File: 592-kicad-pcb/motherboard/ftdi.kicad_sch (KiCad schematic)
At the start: 43 parts, among them J14 USB_B_Micro, U10 FT4232H, U11 74HC595, Y3 12M

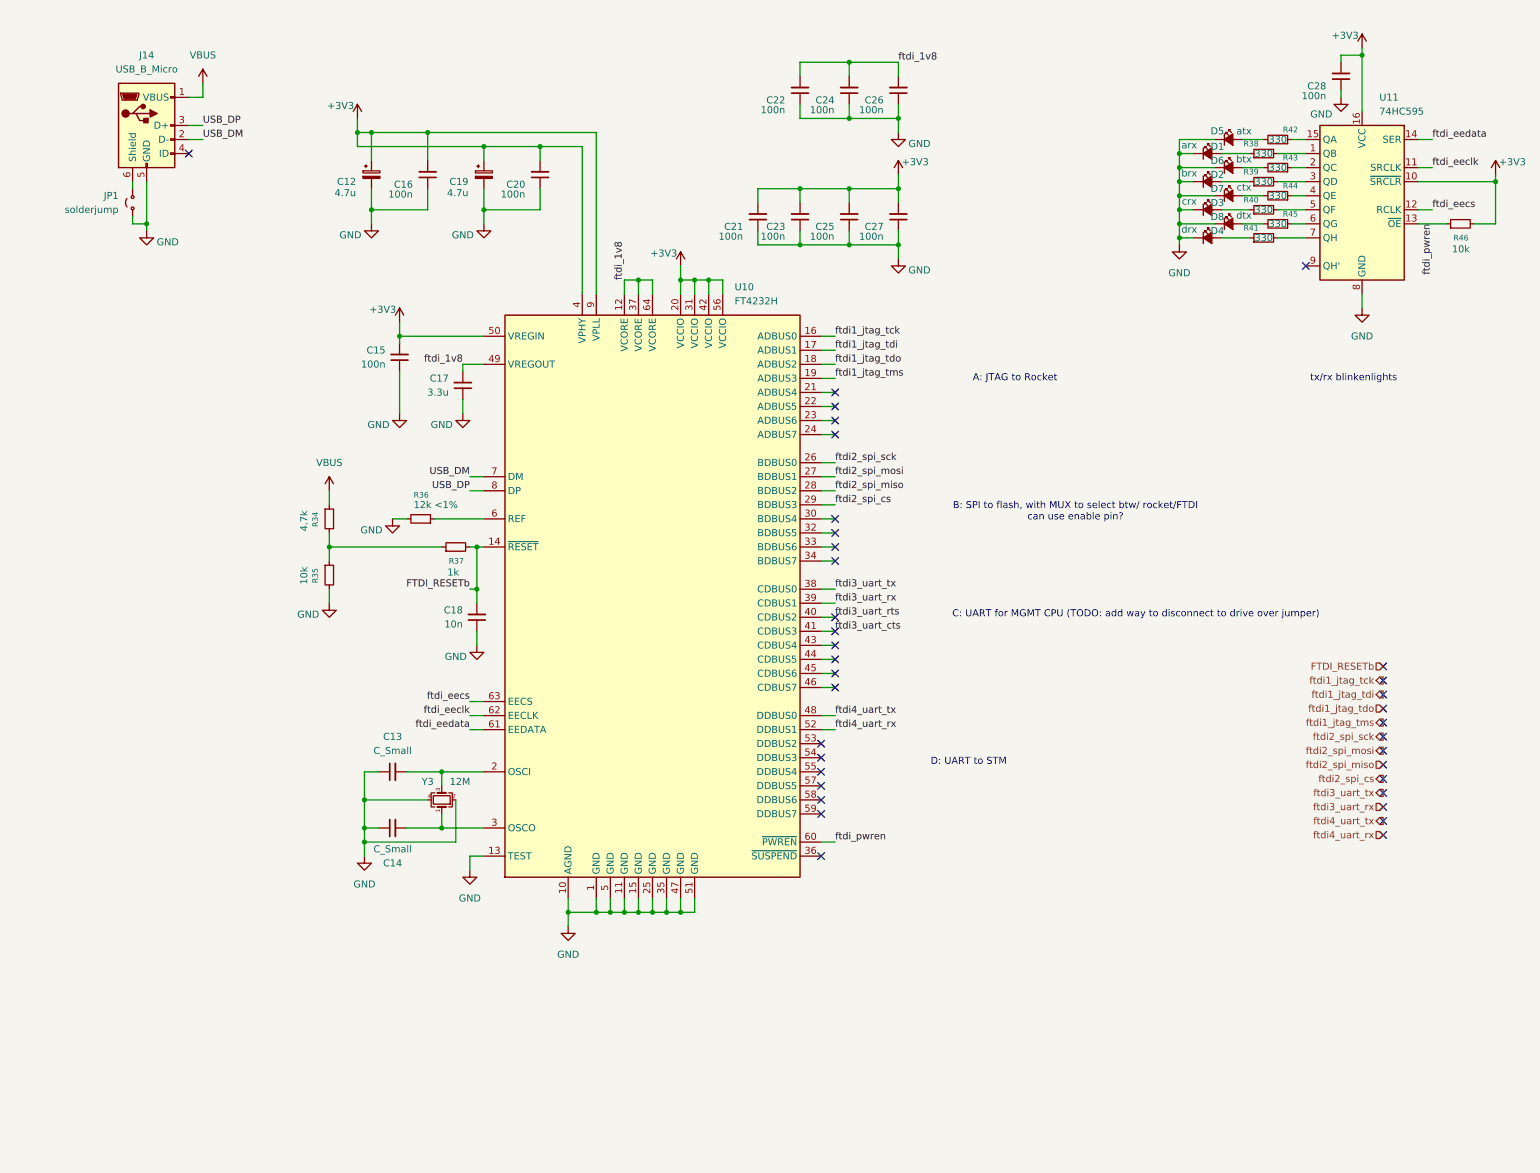
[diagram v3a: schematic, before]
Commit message: add JLC part num for parts, footprints
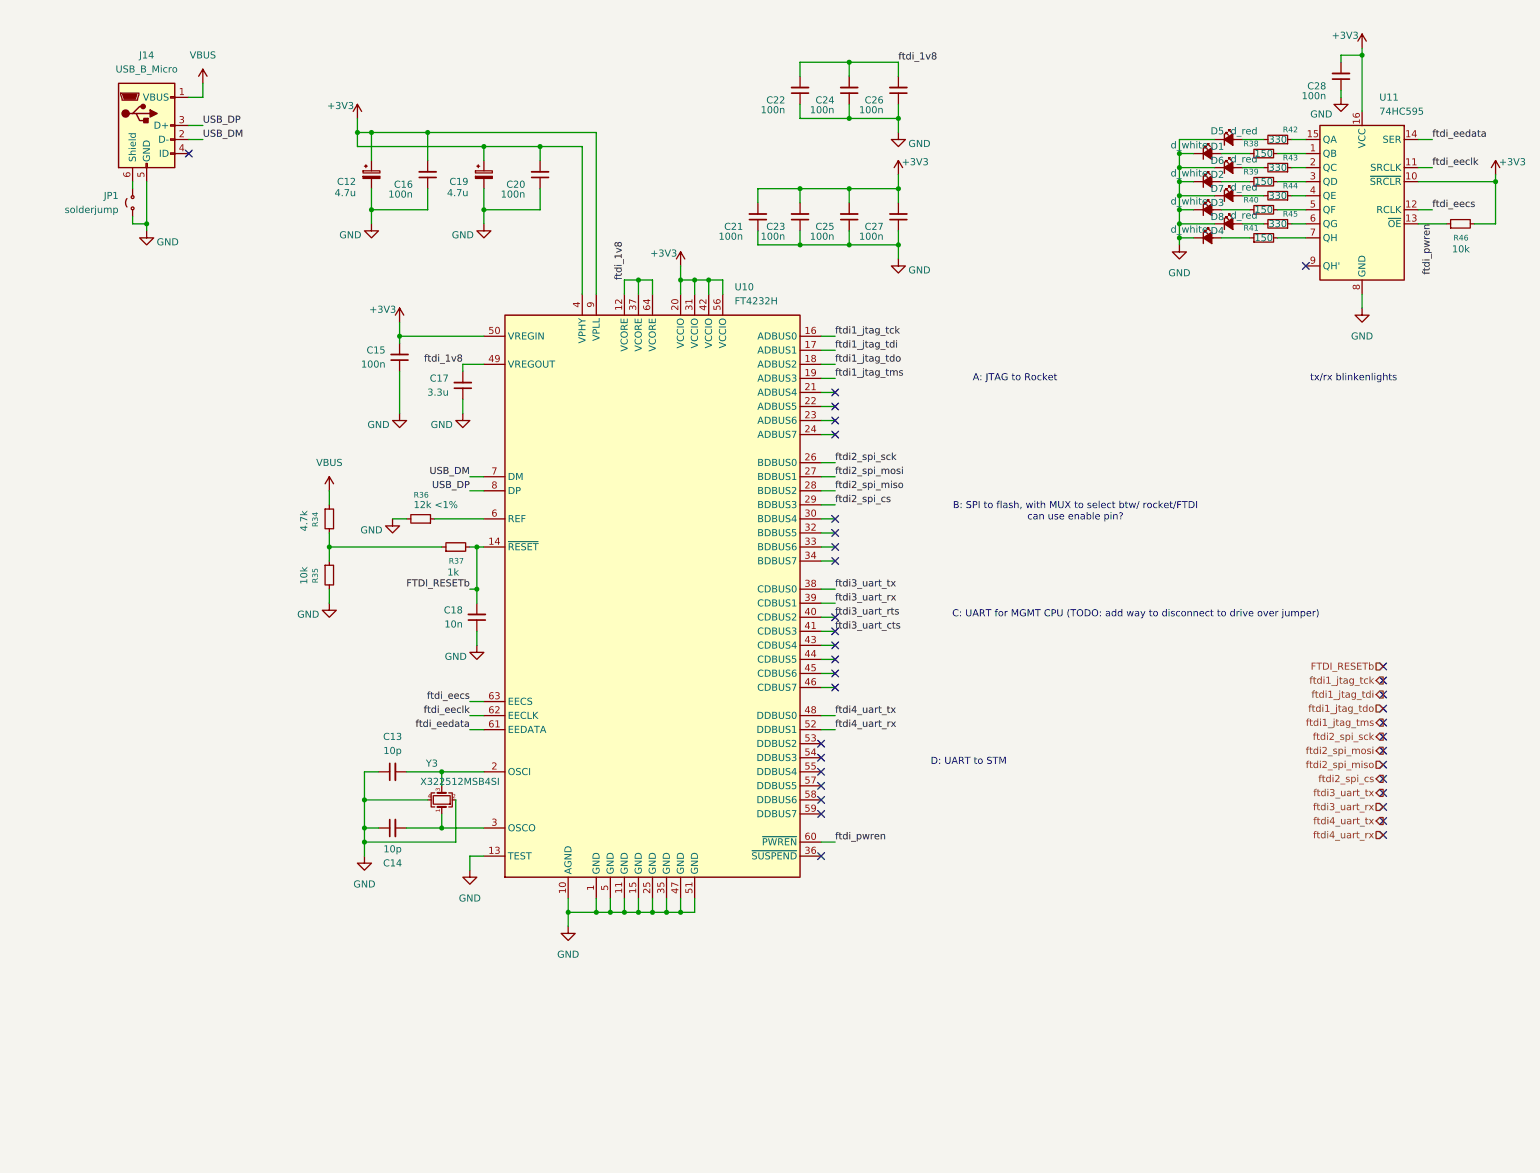
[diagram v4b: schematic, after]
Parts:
- C12, C19: footprint (none) -> Capacitor_Tantalum_SMD:CP_EIA-3216-18_Kemet-A; LCSC (none) -> C7187
- C13, C14: value C_Small -> 10p; footprint (none) -> Capacitor_SMD:C_0402_1005Metric; LCSC (none) -> C32949
- C15, C16, C20, C21, C22, C23, C24, C25, C26, C27, C28: footprint (none) -> Capacitor_SMD:C_0402_1005Metric; LCSC (none) -> C1525
- C17: footprint (none) -> Capacitor_SMD:C_0603_1608Metric; LCSC (none) -> C1588
- C18: footprint (none) -> Capacitor_SMD:C_0402_1005Metric; LCSC (none) -> C15195
- D1: value arx -> d_white; footprint (none) -> Diode_SMD:D_0603_1608Metric; LCSC (none) -> C2290
- D2: value brx -> d_white; footprint (none) -> Diode_SMD:D_0603_1608Metric; LCSC (none) -> C2290
- D3: value crx -> d_white; footprint (none) -> Diode_SMD:D_0603_1608Metric; LCSC (none) -> C2290
- D4: value drx -> d_white; footprint (none) -> Diode_SMD:D_0603_1608Metric; LCSC (none) -> C2290
- D5: value atx -> d_red; footprint (none) -> Diode_SMD:D_0603_1608Metric; LCSC (none) -> C2286
- D6: value btx -> d_red; footprint (none) -> Diode_SMD:D_0603_1608Metric; LCSC (none) -> C2286
- D7: value ctx -> d_red; footprint (none) -> Diode_SMD:D_0603_1608Metric; LCSC (none) -> C2286
- D8: value dtx -> d_red; footprint (none) -> Diode_SMD:D_0603_1608Metric; LCSC (none) -> C2286
- J14: footprint (none) -> Connector_USB:USB_Micro-B_Wuerth_629105150521; LCSC (none) -> C2894326
- JP1: footprint (none) -> Jumper:SolderJumper-2_P1.3mm_Open_RoundedPad1.0x1.5mm
- R34: footprint (none) -> Resistor_SMD:R_0402_1005Metric; LCSC (none) -> C25900
- R35, R46: footprint (none) -> Resistor_SMD:R_0402_1005Metric; LCSC (none) -> C25744
- R36: footprint (none) -> Resistor_SMD:R_0603_1608Metric; LCSC (none) -> C22790
- R37: footprint (none) -> Resistor_SMD:R_0402_1005Metric; LCSC (none) -> C11702
- R38, R39, R40, R41: value 330 -> 150; footprint (none) -> Resistor_SMD:R_0402_1005Metric; LCSC (none) -> C25082
- R42, R43, R44, R45: footprint (none) -> Resistor_SMD:R_0402_1005Metric; LCSC (none) -> C25104
- U10: footprint (none) -> Package_QFP:LQFP-64_10x10mm_P0.5mm; LCSC (none) -> C56742
- U11: footprint (none) -> Package_SO:SOIC-16W_5.3x10.2mm_P1.27mm; LCSC (none) -> C5947
- Y3: value 12M -> X322512MSB4SI; LCSC (none) -> C9002

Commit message: update footprints, final
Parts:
- U11: footprint Package_SO:SOIC-16W_5.3x10.2mm_P1.27mm -> Package_SO:SOIC-16_3.9x9.9mm_P1.27mm

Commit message: updates to routing
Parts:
- renumbered C12 to C14, C13 to C15, C14 to C16, C15 to C17, C16 to C18, C17 to C19, C18 to C20, C19 to C21, C20 to C22, C21 to C23, C22 to C24, C23 to C25, C24 to C26, C25 to C27, C26 to C28, C27 to C29, C28 to C30, J14 to J18, R34 to R35, R35 to R36, R36 to R37, R37 to R38, R38 to R39, R39 to R40, R40 to R41, R41 to R42, R42 to R43, R43 to R44, R44 to R45, R45 to R46, R46 to R47, U10 to U11, U11 to U12

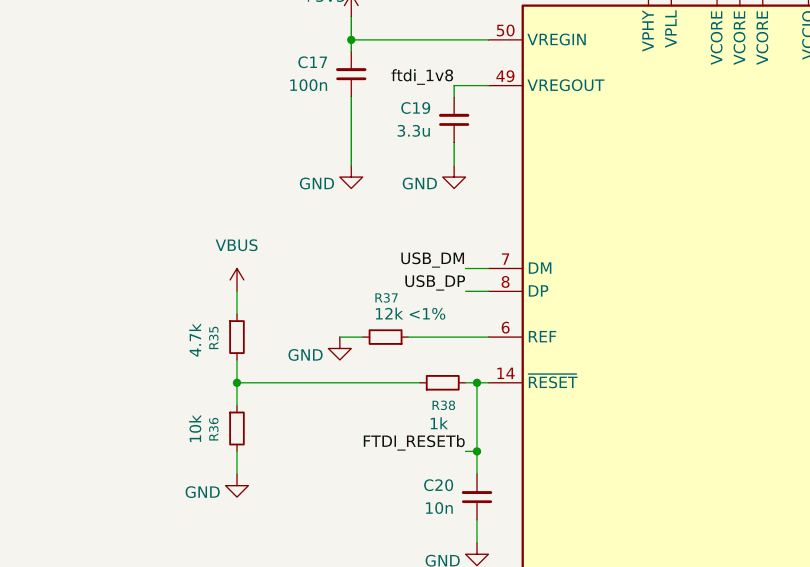
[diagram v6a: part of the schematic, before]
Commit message: more routing progress, add termination resistors
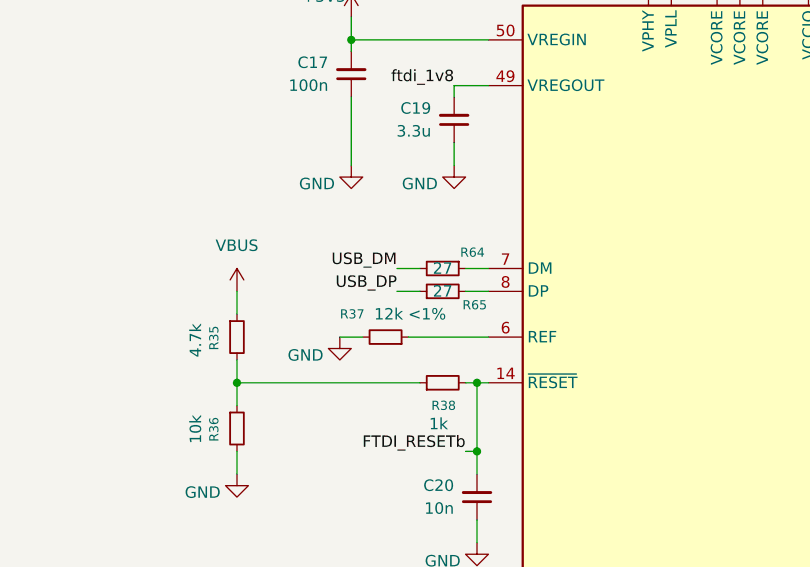
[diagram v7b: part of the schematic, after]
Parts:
- added R64, R65: 27, Resistor_SMD:R_0402_1005Metric, symbol Device:R_Small
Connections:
- net USB_DM: now also R64.2; no longer U11.7 (DM)
- net USB_DP: now also R65.1; no longer U11.8 (DP)
- new net: R65.2, U11.8 (DP)
- new net: R64.1, U11.7 (DM)

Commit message: finalize termination
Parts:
- added D10, D11, D9: D_TVS, symbol Device:D_TVS
- added R92: 10k, symbol Device:R_Small
- added R93, R94, R95, R96, R97: 27, symbol Device:R_Small
- R64, R65: value 27 -> 0
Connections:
- net +3V3: now also R92.1
- net GND: now also D10.1 (A1), D11.1 (A1), D9.1 (A1)
- net USB_DM: now also D9.2 (A2)
- net USB_DP: now also D10.2 (A2)
- net VBUS: now also D11.2 (A2)
- net ftdi1_jtag_tck: now also R96.2; no longer U11.16 (ADBUS0)
- net ftdi1_jtag_tdi: now also R95.2; no longer U11.17 (ADBUS1)
- net ftdi1_jtag_tms: now also R97.2; no longer U11.19 (ADBUS3)
- net ftdi2_spi_cs: now also R92.2
- net ftdi2_spi_mosi: now also R94.2; no longer U11.27 (BDBUS1)
- net ftdi2_spi_sck: now also R93.2; no longer U11.26 (BDBUS0)
- new net: R95.1, U11.17 (ADBUS1)
- new net: R96.1, U11.16 (ADBUS0)
- new net: R97.1, U11.19 (ADBUS3)
- new net: R93.1, U11.26 (BDBUS0)
- new net: R94.1, U11.27 (BDBUS1)
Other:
- note added: "input impedance ~45ohm trace impedance ~72ohm"
- moved on the sheet: J18, JP1
